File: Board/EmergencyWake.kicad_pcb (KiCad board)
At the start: 2 copper layers, 100 x 67 mm, 138 parts, among them J1 USB_C_Receptacle_USB2.0, J2 Micro_SD_Card_Det, J3 Conn_01x03, J4 Conn_01x02, J5 Conn_01x04, J6 Conn_01x04, J7 Conn_01x02, J8 Conn_01x04, J9 Conn_01x04, Q1 AO3400A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

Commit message: [Board] Did some routing
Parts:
- moved R38 2.00 mm to (178.5, 140.0)
- moved R39 2.00 mm to (176.5, 140.0)
- moved REF** 0.20 mm to (140.9, 142.0)
- moved C28 0.11 mm to (166.8, 103.8)
- moved R29 0.11 mm to (166.8, 105.8)
- moved C29 0.10 mm to (174.8, 103.8)
- moved R30 0.10 mm to (174.8, 105.8)
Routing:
- net GND: track 56.2 -> 351.4 mm
- net VCC: track 30.3 -> 133.1 mm, vias 0 -> 5
- net +5V: track 30.2 -> 104.7 mm, vias 0 -> 2
- net Net-(DISP1-Pad32): track 0.00 -> 66.8 mm, vias 0 -> 1
- net Vdrive: track 0.00 -> 51.8 mm
- net Net-(D5-Pad2): track 25.9 -> 76.0 mm, vias 0 -> 2
- net /BUZZER: track 0.00 -> 48.8 mm
- net Net-(C13-Pad1): track 0.00 -> 30.2 mm
- net /DCF_PON: track 0.00 -> 27.7 mm
- net GNDD: track 2.00 -> 26.0 mm, vias 19 -> 16
- net /VFD_GRID_2_HV: track 0.00 -> 22.2 mm
- net Net-(DISP1-Pad1): track 0.00 -> 21.7 mm, vias 0 -> 1
- net /SD_D0: track 0.00 -> 21.1 mm
- net Net-(R38-Pad1): track 0.00 -> 19.7 mm
- net /SD_CK: track 0.00 -> 16.5 mm
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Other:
- board text added: "-VDC"
- board text added: "DCDC in"

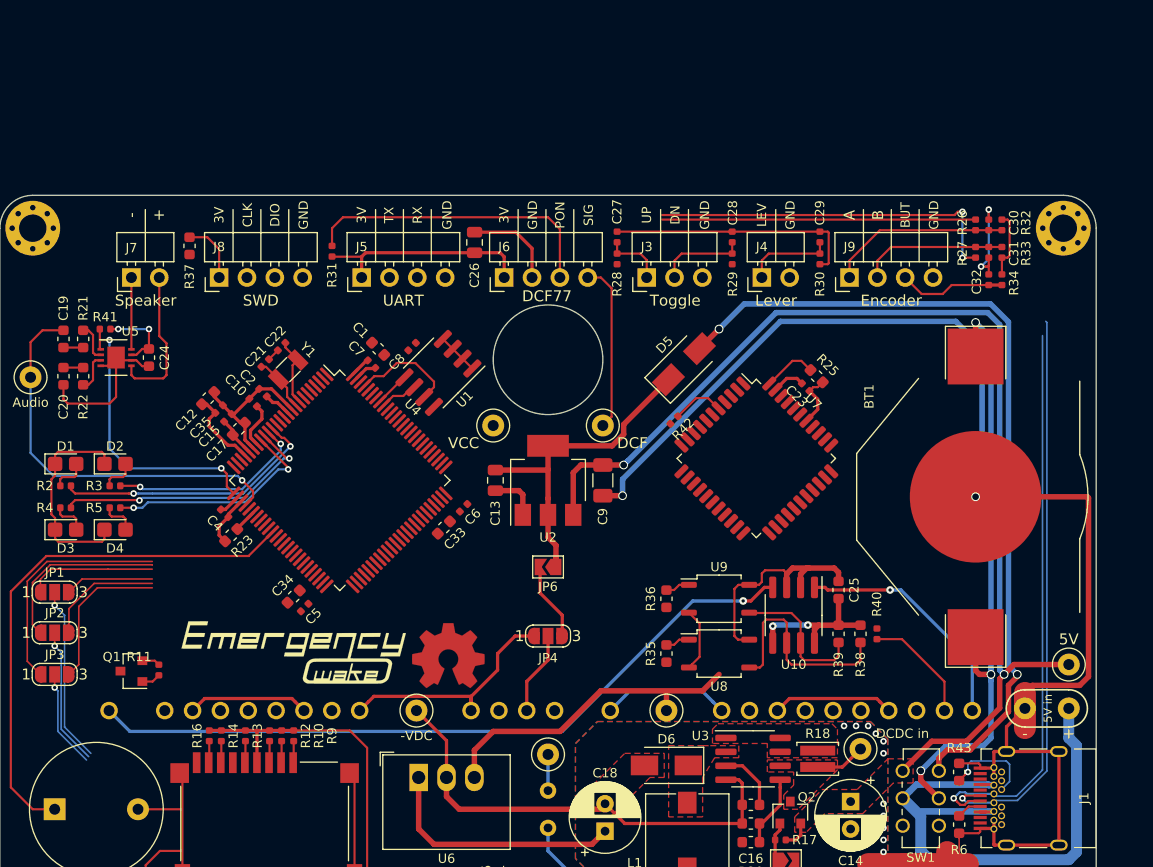
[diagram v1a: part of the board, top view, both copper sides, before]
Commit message: [Board] Removed solder paste for not-fitted components. Added I2C for proximity sensor. Moved SWD and UART connector
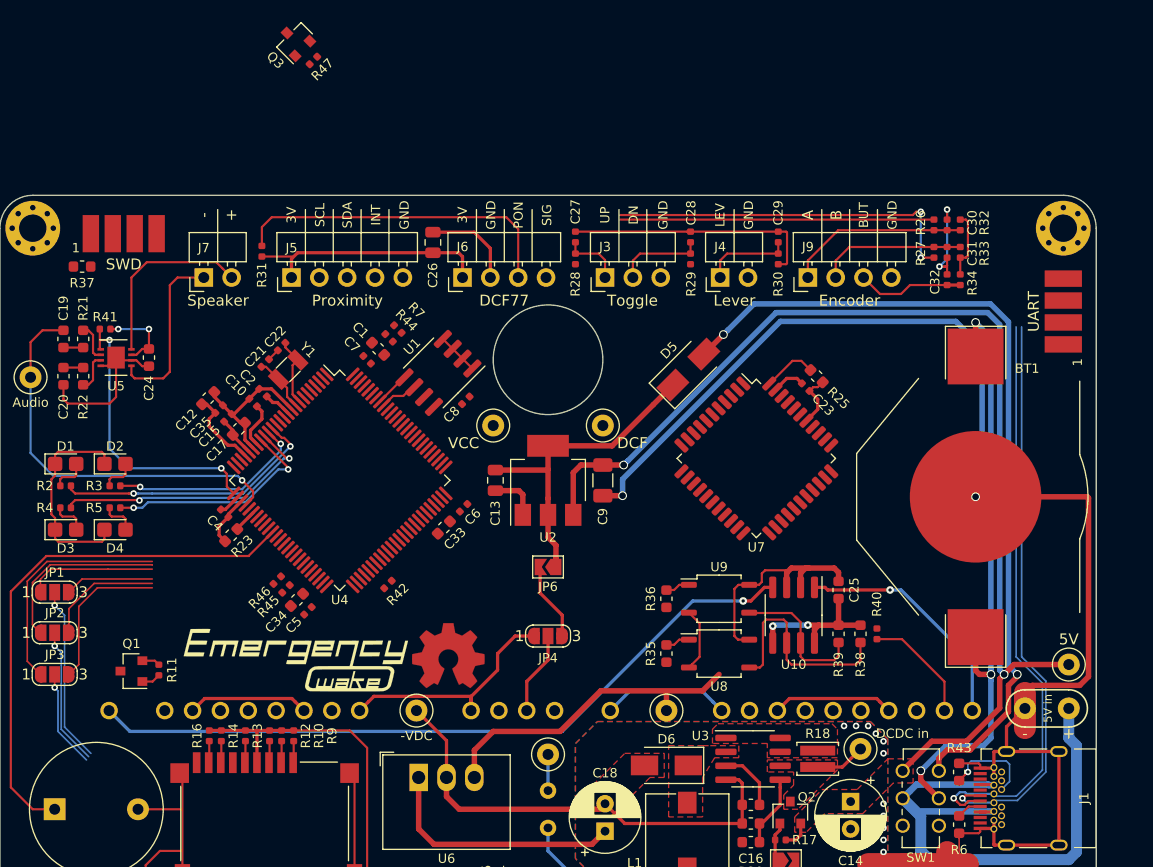
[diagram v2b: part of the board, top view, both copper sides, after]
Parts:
- added J10: Conn_01x04, WR-WTB:WR-WTB 2.00mm SMT Male Horizontal Shrouded Header 4 Pins, F.Cu at (197.0, 110.6)
- added Q3: AO3400A, Package_TO_SOT_SMD:SOT-23, F.Cu at (126.9, 85.9)
- added R44: 10k, Resistor_SMD:R_0402_1005Metric, F.Cu at (135.5, 113.0)
- added R45: 10k, Resistor_SMD:R_0402_1005Metric, F.Cu at (126.1, 135.9)
- added R46: 10k, Resistor_SMD:R_0402_1005Metric, F.Cu at (125.3, 135.1)
- added R47: 100k, Resistor_SMD:R_0402_1005Metric, F.Cu at (128.6, 87.7)
- added R7: 10k, Resistor_SMD:R_0402_1005Metric, F.Cu at (136.3, 112.2)
- J5: value Conn_01x04 -> Conn_01x05; footprint Connector_PinHeader_2.54mm:PinHeader_1x04_P2.54mm_Horizontal -> Connector_PinHeader_2.54mm:PinHeader_1x05_P2.54mm_Horizontal
- J8: footprint Connector_PinHeader_2.54mm:PinHeader_1x04_P2.54mm_Horizontal -> WR-WTB:WR-WTB 2.00mm SMT Male Horizontal Shrouded Header 4 Pins
- TP11: value TestPoint -> DCF
- moved R42 30.1 mm to (135.4, 135.5), turned to 45 degrees
- moved R37 9.98 mm to (107.5, 106.5), turned to 0 degrees
- moved J8 9.58 mm to (111.3, 103.5), turned to 0 degrees
- moved C8 6.93 mm to (142.5, 118.7)
- moved J7 6.60 mm to (118.6, 107.5)
- moved J5 6.40 mm to (126.6, 107.5)
- moved R31 6.40 mm to (123.9, 105.1)
- moved C26 3.80 mm to (139.5, 104.3)
- moved C27 3.80 mm to (152.5, 103.8)
- moved C28 3.80 mm to (163.0, 103.8)
- moved C29 3.80 mm to (171.0, 103.8)
- moved J3 3.80 mm to (155.2, 107.5)
- moved J4 3.80 mm to (165.7, 107.5)
- moved J6 3.80 mm to (142.2, 107.5)
- moved J9 3.80 mm to (173.7, 107.5)
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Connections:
- J5 pad 2: /UART_TX -> /I2C_SCL
- J5 pad 3: /UART_RX -> /I2C_SDA
- J5 pad 4: GND -> /I2C_INT
- J7 pad 1: /SP- -> /SP+
- J7 pad 2: /SP+ -> /SP-
- U4 pad 35: Net-(U4-Pad35) -> /I2C_INT
- U4 pad 47: Net-(U4-Pad47) -> /I2C_SCL
- U4 pad 48: Net-(U4-Pad48) -> /I2C_SDA
- U4 pad 56: Net-(U4-Pad56) -> /I2C_EN
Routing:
- net /DCF_SIG: track 15.4 -> 0.00 mm
- net /SP-: track 6.55 -> 16.8 mm
- net /EEPROM_NWC: track 9.70 -> 0.00 mm
- net Net-(J8-Pad1): track 5.75 -> 0.00 mm
- net /VFD_DOUT: track 4.79 -> 0.00 mm
- net /DCF_PON: track 27.7 -> 30.3 mm
- net /SP+: track 13.5 -> 16.0 mm
- net GND: track 351.4 -> 349.3 mm
- net /USB_DP: track 51.9 -> 53.7 mm
- net VCC: track 133.1 -> 133.9 mm
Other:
- board text added: "Proximity"

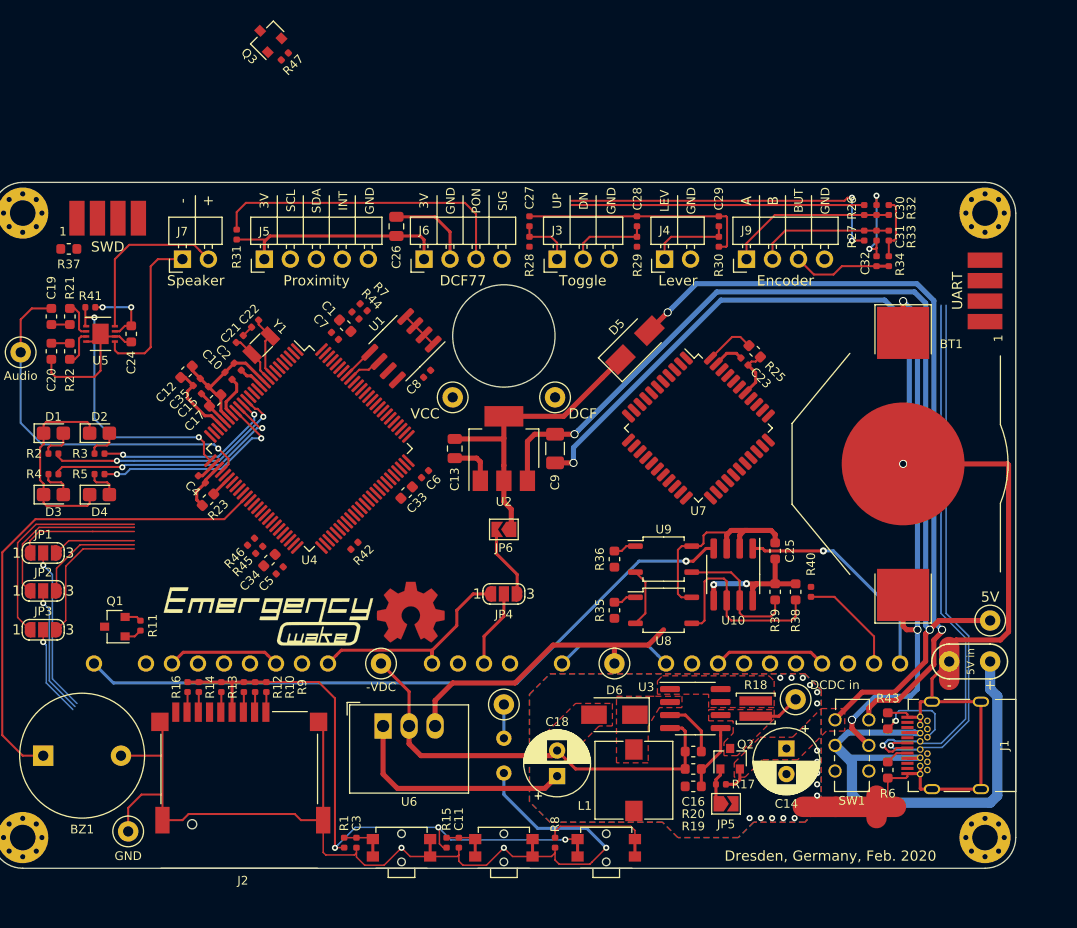
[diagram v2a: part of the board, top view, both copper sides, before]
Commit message: [Board] More routing done
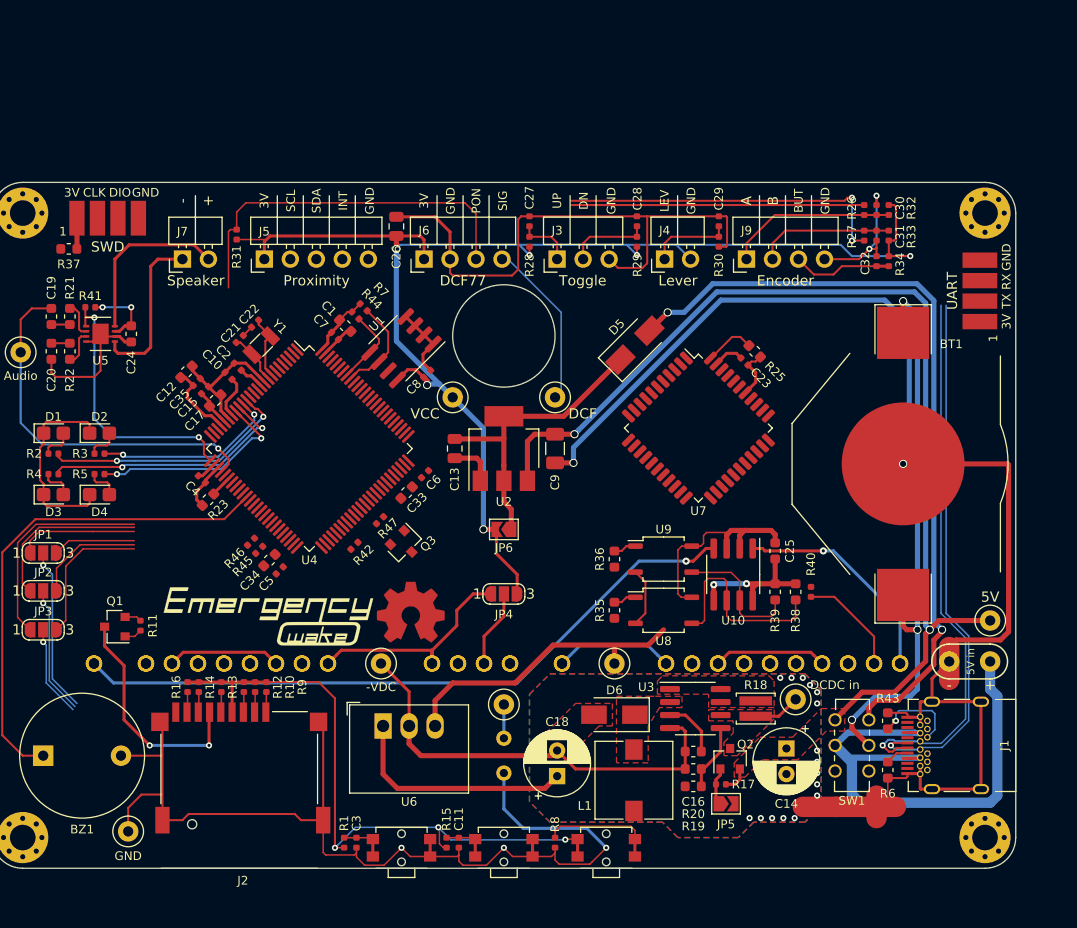
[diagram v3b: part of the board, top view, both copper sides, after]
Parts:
- added DISP1: FUTABA_4-LT-46ZB3, VFD:FUTABA_4-LT-46ZB3, B.Cu at (150.0, 126.0)
- moved Q3 51.3 mm to (140.3, 135.4), turned to 315 degrees
- moved R47 46.2 mm to (137.9, 133.0), turned to 45 degrees
- moved J10 0.50 mm to (196.5, 110.6)
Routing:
- net VCC: track 133.9 -> 238.5 mm, vias 5 -> 11
- net GND: track 349.3 -> 385.0 mm
- net Net-(J2-Pad6): track 0.00 -> 22.5 mm, vias 0 -> 2
- net /DCF_SIG: track 0.00 -> 16.5 mm
- net /DCF_PON: track 30.3 -> 36.7 mm
- net /EEPROM_SCL: track 3.42 -> 9.60 mm
- net /EEPROM_SDA: track 3.31 -> 7.76 mm
- net Net-(J8-Pad1): track 0.00 -> 3.01 mm
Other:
- board text added: "3V"
- board text added: "CLK"
- board text added: "DIO"
- board text added: "RX"
- board text added: "TX"
- board text removed: "Dresden, Germany, Feb. 2020"

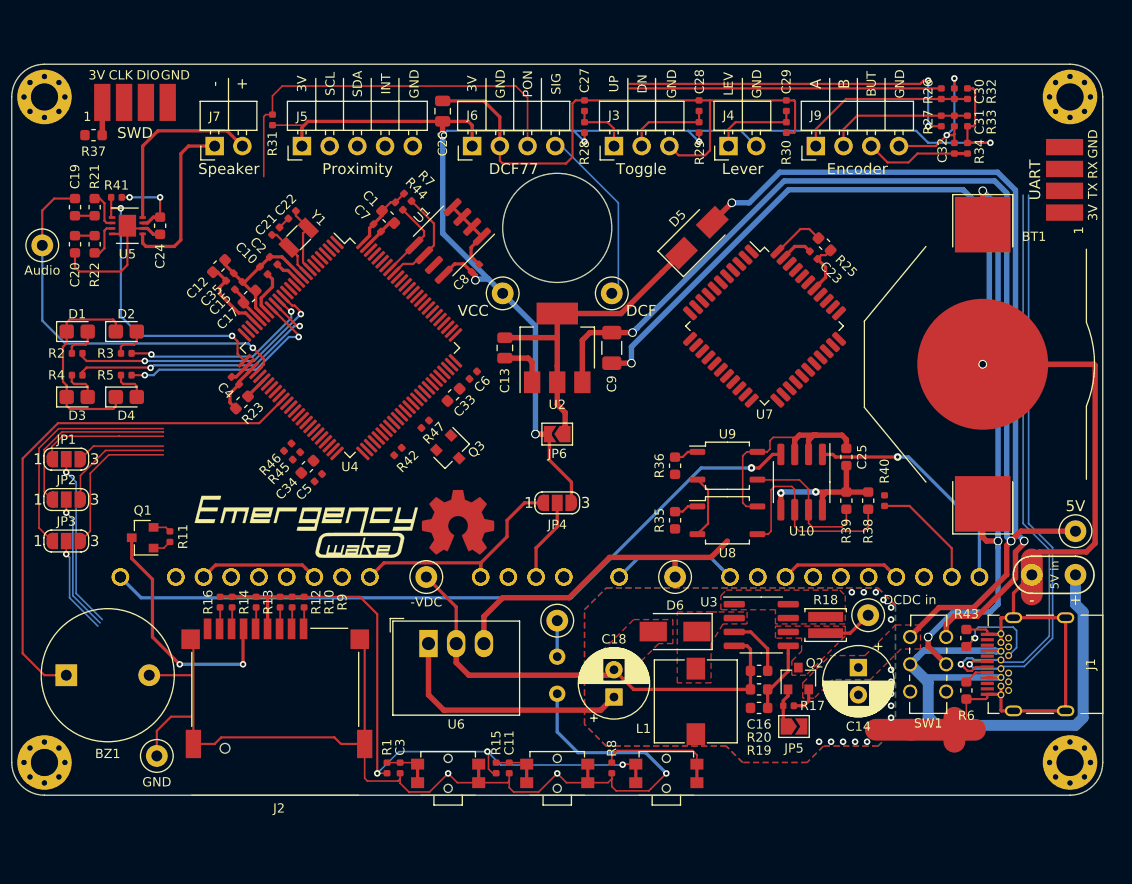
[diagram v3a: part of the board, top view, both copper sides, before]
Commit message: [Board] More routing
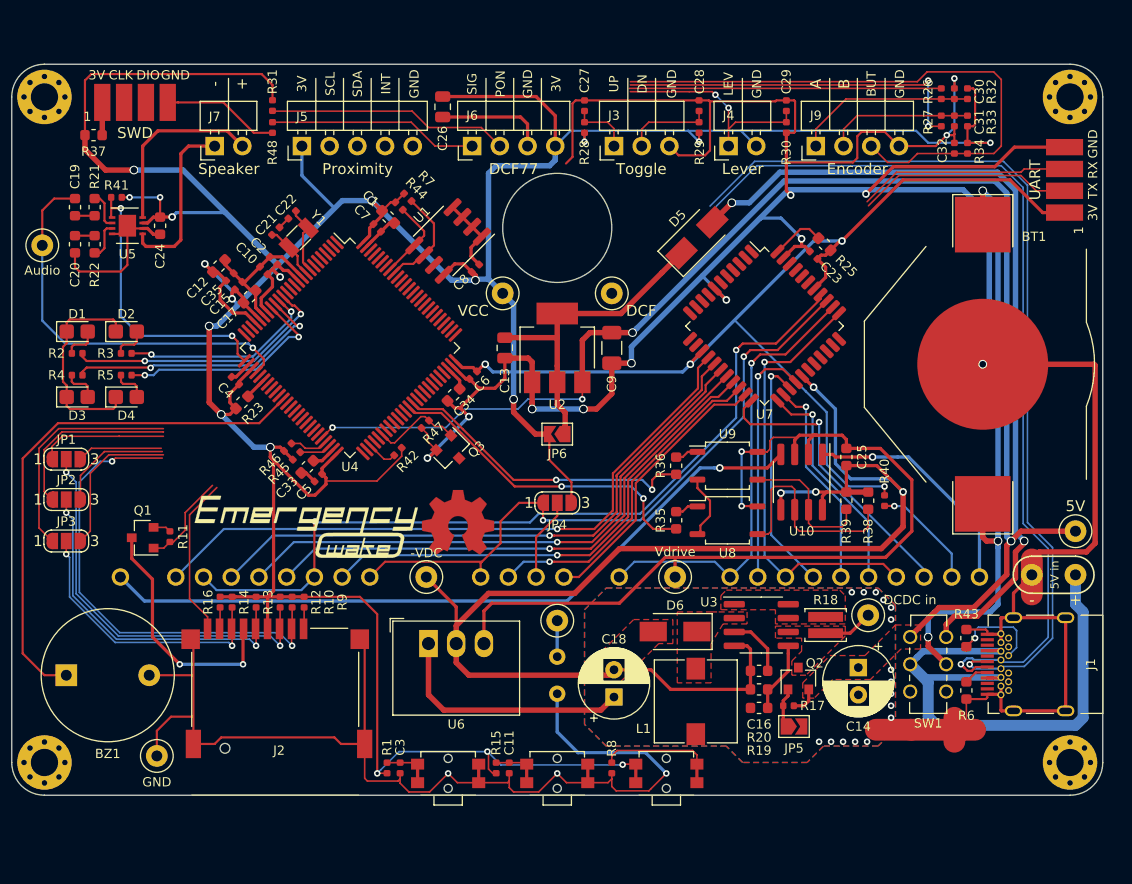
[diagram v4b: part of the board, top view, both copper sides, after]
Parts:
- removed the DISP1 at (150.0, 126.0) (x2)
- added DISP1: FUTABA_4-LT-46ZB3, VFD:FUTABA_4-LT-46ZB3, B.Cu at (150.0, 126.0)
- added R48: 100k, Resistor_SMD:R_0402_1005Metric, F.Cu at (123.9, 105.8)
- moved C33 14.9 mm to (127.1, 136.9)
- moved C34 14.9 mm to (140.5, 130.3)
- moved R31 1.31 mm to (123.9, 103.8), turned to 90 degrees
- moved C26 0.40 mm to (139.5, 103.9), turned to 270 degrees
- moved R35 0.10 mm to (160.9, 141.8)
- moved R36 0.10 mm to (160.9, 136.8)
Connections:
- J6 pad 1: VCC -> /DCF_SIG
- J6 pad 2: GND -> /DCF_PON
- J6 pad 3: /DCF_PON -> GND
- J6 pad 4: /DCF_SIG -> VCC
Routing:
- net VCC: track 238.5 -> 469.1 mm, vias 11 -> 23
- net GND: track 385.0 -> 476.7 mm, vias 7 -> 15
- net -VDC: track 56.5 -> 128.8 mm, vias 2 -> 4
- net /VFD_GRID_1_HV: track 11.1 -> 75.2 mm, vias 0 -> 2
- net Net-(DISP1-Pad30): track 0.00 -> 60.2 mm, vias 0 -> 1
- net Net-(DISP1-Pad28): track 0.00 -> 55.1 mm, vias 0 -> 1
- net Net-(DISP1-Pad27): track 0.00 -> 52.5 mm, vias 0 -> 1
- net Net-(DISP1-Pad26): track 0.00 -> 50.0 mm, vias 0 -> 1
- net Net-(DISP1-Pad24): track 0.00 -> 45.2 mm, vias 0 -> 1
- net /ENC_BUT: track 9.78 -> 53.9 mm
- net /SD_CS: track 1.99 -> 43.8 mm, vias 0 -> 2
- net /VFD_GRID_2_HV: track 22.2 -> 60.5 mm, vias 0 -> 2
- net /USB_DM: track 52.2 -> 84.8 mm
- net /USB_DP: track 53.7 -> 85.3 mm
- net Net-(DISP1-Pad18): track 0.00 -> 30.3 mm, vias 0 -> 1
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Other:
- board text added: "Vdrive"
